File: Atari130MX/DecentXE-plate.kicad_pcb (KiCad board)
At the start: 2 copper layers, 329.2 x 129.3 mm, 70 parts, among them SW0 SW_Push_45deg, SW1 SW_Push_45deg, SW2 SW_Push_45deg, SW3 SW_Push_45deg, SW4 SW_Push_45deg, SW5 SW_Push_45deg, SW6 SW_Push_45deg, SW7 SW_Push_45deg, SW8 SW_Push_45deg, SW9 SW_Push_45deg

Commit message: New layout prototype for PCB and plate
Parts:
- moved G*** 3.99 mm to (336.9, 144.2)

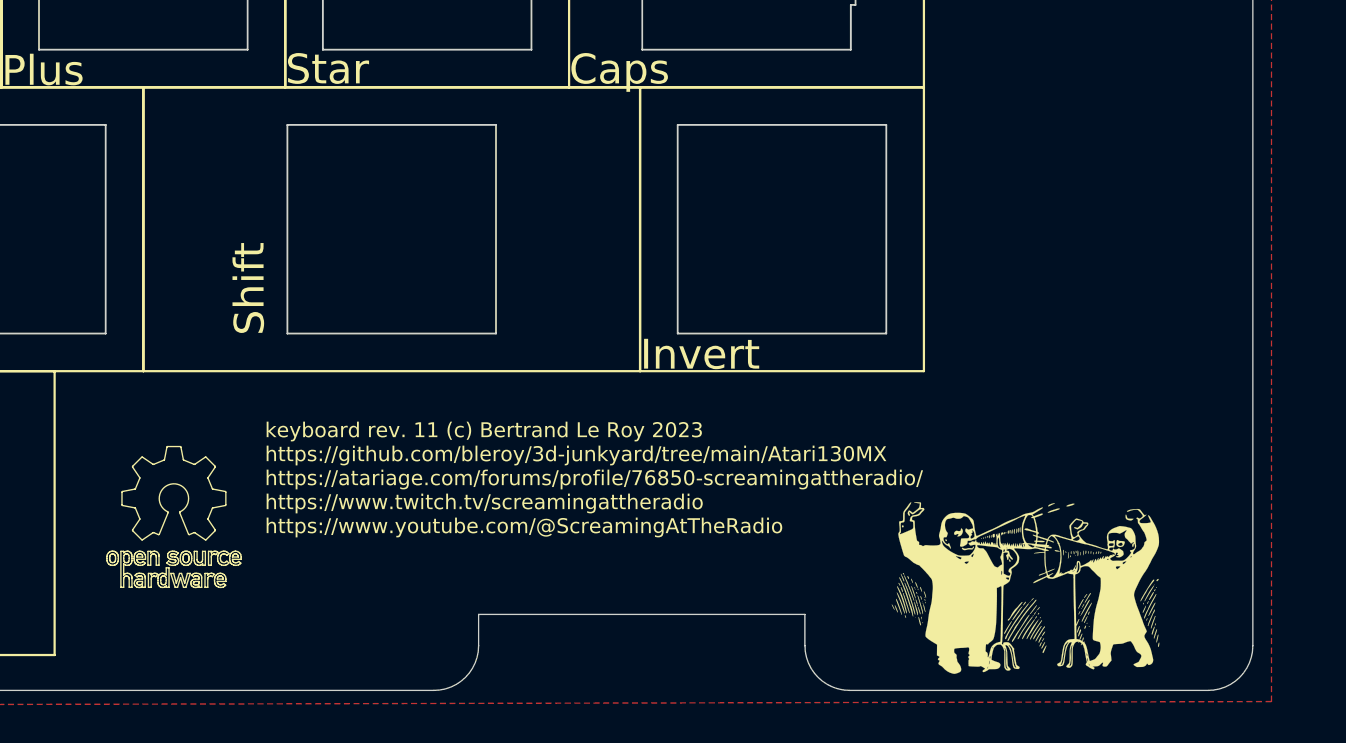
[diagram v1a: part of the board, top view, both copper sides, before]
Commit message: Small cosmetic plate changes
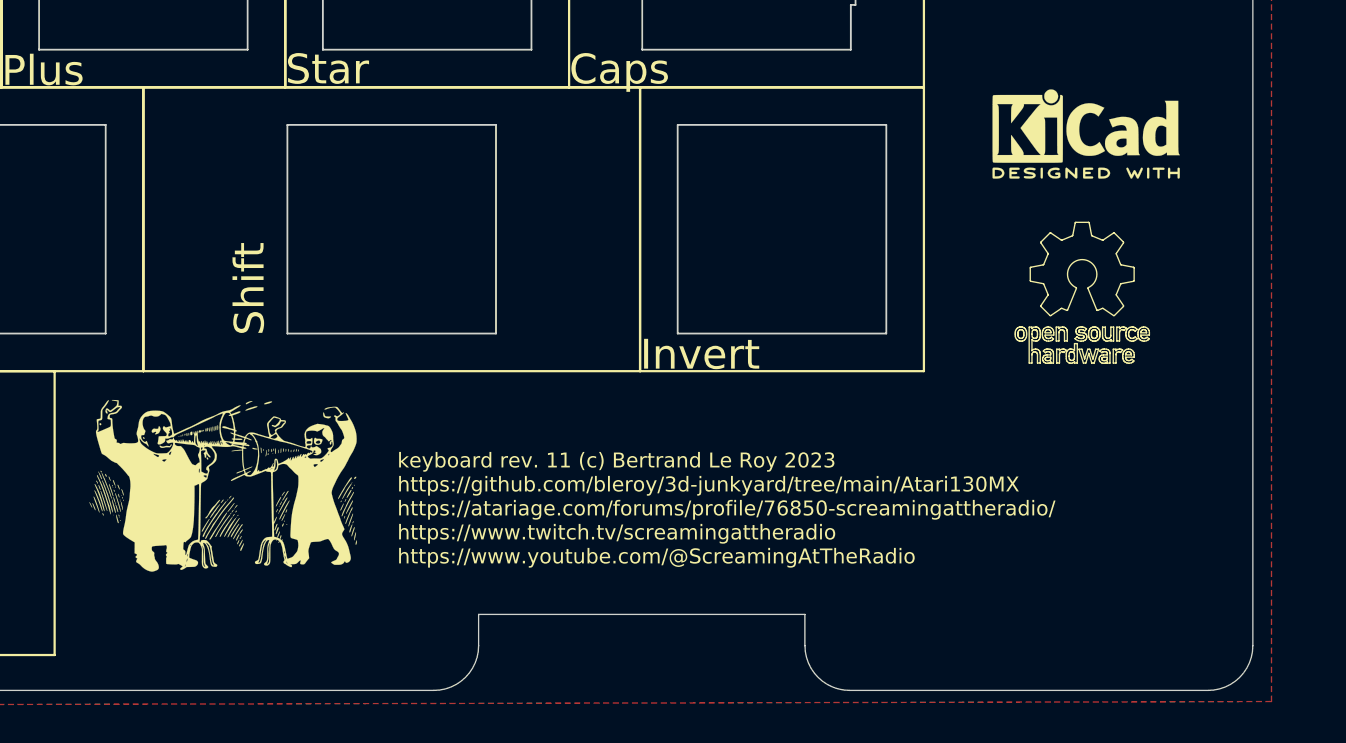
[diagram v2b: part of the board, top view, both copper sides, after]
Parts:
- added REF**: KiCad-Logo2_5mm_SilkScreen, Symbol:KiCad-Logo2_5mm_SilkScreen, F.Cu at (340.9, 114.8)
- moved REF** 62.8 mm to (340.6, 124.1)
- moved G*** 54.3 mm to (283.1, 137.3)

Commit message: Use the right font for logos
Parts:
- removed the G*** at (187.5, 91.7)
- removed the G*** at (54.4, 27.7)
- added G***: LOGO, LOGO, F.Cu at (55.1, 29.5)
- added G***: LOGO, LOGO, F.Cu at (187.5, 91.2)

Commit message: Add vintage stabilizer holes to plate.
SVG file is also updated
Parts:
- SWBrk2: footprint Atari130MX:MX-1-25U-Hole -> Atari130MX:MX-1-25U-RightOfSpace-Hole
- SWCtl1: footprint Atari130MX:MX-1-25U-Hole -> Atari130MX:MX-1-25U-LeftOfSpace-Hole

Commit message: Misc updates
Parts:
- moved G*** 2.14 mm to (187.4, 89.1)
